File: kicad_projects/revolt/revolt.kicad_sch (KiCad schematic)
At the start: 0 parts

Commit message: add matrix to the schematic, minus the net names
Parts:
- added D1, D10, D11, D12, D13, D14, D15, D16, D17, D18, D19, D2, D20, D21, D22, D23, D24, D25, D26, D27, D28, D29, D3, D30, D31, D32, D33, D34, D4, D5, D6, D7, D8, D9: D, symbol Device:D
- added S1, S10, S11, S12, S13, S14, S15, S16, S17, S18, S19, S2, S20, S21, S22, S23, S24, S25, S26, S27, S28, S29, S3, S30, S31, S32, S33, S34, S4, S5, S6, S7, S8, S9: SW_Push_45deg, symbol Switch:SW_Push_45deg
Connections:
- new net: D12.1 (K), D17.1 (K), D2.1 (K), D21.1 (K), D25.1 (K), D33.1 (K), D7.1 (K)
- new net: D33.2 (A), S33.2
- new net: S25.1, S26.1, S27.1, S28.1, S32.1
- new net: D25.2 (A), S25.2
- new net: D14.1 (K), D19.1 (K), D23.1 (K), D27.1 (K), D30.1 (K), D4.1 (K), D9.1 (K)
- new net: D30.2 (A), S30.2
- new net: S10.1, S6.1, S7.1, S8.1, S9.1
- new net: D10.2 (A), S10.2
- new net: S1.1, S2.1, S3.1, S4.1, S5.1
- new net: D5.2 (A), S5.2
- new net: S11.1, S12.1, S13.1, S14.1, S15.1
- new net: D15.2 (A), S15.2
- new net: S21.1, S22.1, S23.1, S24.1, S31.1
- new net: D22.2 (A), S22.2
- new net: D4.2 (A), S4.2
- new net: D3.2 (A), S3.2
- new net: D28.2 (A), S28.2
- new net: D14.2 (A), S14.2
- new net: D13.1 (K), D18.1 (K), D22.1 (K), D26.1 (K), D29.1 (K), D3.1 (K), D8.1 (K)
- new net: D29.2 (A), S29.2
- new net: S29.1, S30.1, S33.1, S34.1
- new net: D32.2 (A), S32.2
- new net: D1.1 (K), D11.1 (K), D16.1 (K), D31.1 (K), D32.1 (K), D34.1 (K), D6.1 (K)
- new net: D11.2 (A), S11.2
- new net: S16.1, S17.1, S18.1, S19.1, S20.1
- new net: D16.2 (A), S16.2
- new net: D21.2 (A), S21.2
- new net: D17.2 (A), S17.2
- new net: D27.2 (A), S27.2
- new net: D10.1 (K), D15.1 (K), D20.1 (K), D24.1 (K), D28.1 (K), D5.1 (K)
- new net: D23.2 (A), S23.2
- new net: D20.2 (A), S20.2
- new net: D2.2 (A), S2.2
- new net: D6.2 (A), S6.2
- new net: D31.2 (A), S31.2
- new net: D12.2 (A), S12.2
- new net: D34.2 (A), S34.2
- new net: D26.2 (A), S26.2
- new net: D13.2 (A), S13.2
- new net: D9.2 (A), S9.2
- new net: D18.2 (A), S18.2
- new net: D7.2 (A), S7.2
- new net: D19.2 (A), S19.2
- new net: D24.2 (A), S24.2
- new net: D1.2 (A), S1.2
- new net: D8.2 (A), S8.2

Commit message: fixed pcb and schematic
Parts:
- D1, D10, D11, D12, D13, D14, D15, D16, D17, D18, D19, D2, D20, D21, D22, D23, D24, D25, D26, D27, D28, D29, D3, D30, D31, D32, D33, D34, D4, D5, D6, D7, D8, D9: value D -> ~; footprint (none) -> ComboDiode
- S1, S10, S11, S12, S13, S14, S15, S16, S17, S18, S19, S2, S20, S21, S22, S23, S24, S25, S26, S27, S28, S29, S3, S30, S31, S32, S33, S34, S4, S5, S6, S7, S8, S9: value SW_Push_45deg -> ~; footprint (none) -> keyswitches:SW_PG1350_reversible
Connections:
- net ROW3: now reaches D12.1 (K), D17.1 (K), D2.1 (K), D21.1 (K), D25.1 (K), D33.1 (K), D7.1 (K)
- net COL5: now reaches S25.1, S26.1, S27.1, S28.1, S32.1
- net ROW1: now reaches D14.1 (K), D19.1 (K), D23.1 (K), D27.1 (K), D30.1 (K), D4.1 (K), D9.1 (K)
- net COL1: now reaches S10.1, S6.1, S7.1, S8.1, S9.1
- net COL0: now reaches S1.1, S2.1, S3.1, S4.1, S5.1
- net COL2: now reaches S11.1, S12.1, S13.1, S14.1, S15.1
- net COL4: now reaches S21.1, S22.1, S23.1, S24.1, S31.1
- net ROW2: now reaches D13.1 (K), D18.1 (K), D22.1 (K), D26.1 (K), D29.1 (K), D3.1 (K), D8.1 (K)
- net COL6: now reaches S29.1, S30.1, S33.1, S34.1
- net ROW4: now reaches D1.1 (K), D11.1 (K), D16.1 (K), D31.1 (K), D32.1 (K), D34.1 (K), D6.1 (K)
- net COL3: now reaches S16.1, S17.1, S18.1, S19.1, S20.1
- net ROW0: now reaches D10.1 (K), D15.1 (K), D20.1 (K), D24.1 (K), D28.1 (K), D5.1 (K)
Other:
- moved on the sheet: D1, D10, D11, D12, D13, D14, D15, D16, D17, D18, D19, D2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

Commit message: todos, remove fp info cache
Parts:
- added J1: IDC-Header_2x07_P2.54mm_Vertical, Connector_IDC:IDC-Header_2x07_P2.54mm_Vertical, symbol Connector_Generic:Conn_02x07_Odd_Even
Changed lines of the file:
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@@
     (stroke (width 0) (type default))
+  )
+  (global_label "GND" (shape input) (at 217.17 31.75 0) (fields_autoplaced)
+    (effects (font (size 1.27 1.27)) (justify left))
+    (property "Intersheetrefs" "${INTERSHEET_REFS}" (at 224.0257 31.75 0)
+      (effects (font (size 1.27 1.27)) (justify left) hide)
+    )
+  )
+  (global_label "5V" (shape input) (at 196.85 31.75 180) (fields_autoplaced)
+    (effects (font (size 1.27 1.27)) (justify right))
+    (property "Intersheetrefs" "${INTERSHEET_REFS}" (at 191.5667 31.75 0)
+      (effects (font (size 1.27 1.27)) (justify right) hide)
+    )
   )
   (hierarchical_label "COL3" (shape input) (at 88.9 25.4 90) (fields_autoplaced)
@@
         )
       )
+    )
+  )
+  (symbol (lib_id "Connector_Generic:Conn_02x07_Odd_Even") (at 205.74 39.37 0) (unit 1)
+    (in_bom yes) (on_board yes) (dnp no) (fields_autoplaced)
+    (property "Reference" "J1" (at 207.01 25.4 0)
+      (effects (font (size 1.27 1.27)))
+    )
+    (property "Value" "IDC-Header_2x07_P2.54mm_Vertical" (at 207.01 27.94 0)
+      (effects (font (size 1.27 1.27)))
+    )
+    (property "Footprint" "Connector_IDC:IDC-Header_2x07_P2.54mm_Vertical" (at 205.74 39.37 0)
+      (effects (font (size 1.27 1.27)) hide)
+    )
+    (property "Datasheet" "~" (at 205.74 39.37 0)
+      (effects (font (size 1.27 1.27)) hide)
+    )
+    (pin "1")
+    (pin "11")
+    (pin "10")
+    (pin "12")
+    (pin "13")
+    (pin "14")
+    (pin "2")
+    (pin "3")
+    (pin "4")
+    (pin "5")
+    (pin "6")
+    (pin "7")
+    (pin "8")
+    (pin "9")
+    (instances
+      (project "revolt"
+        (path "/b3b33ac8-110b-40a8-aa44-efaba806d054"
+          (reference "J1") (unit 1)
+        )
+      )

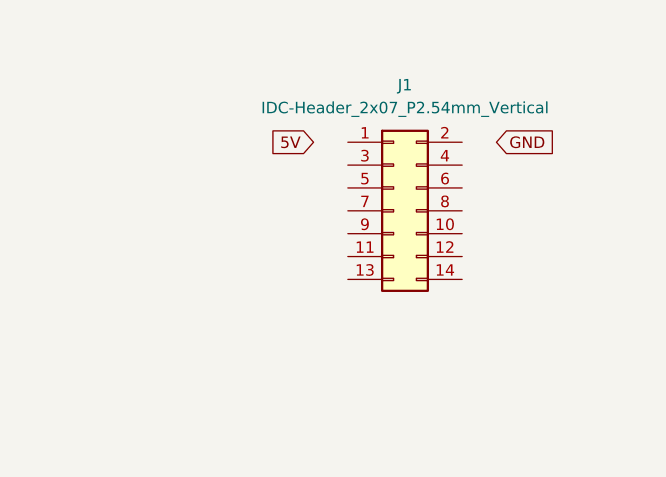
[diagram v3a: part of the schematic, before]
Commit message: Base design, need to unify and double-check DRD rules
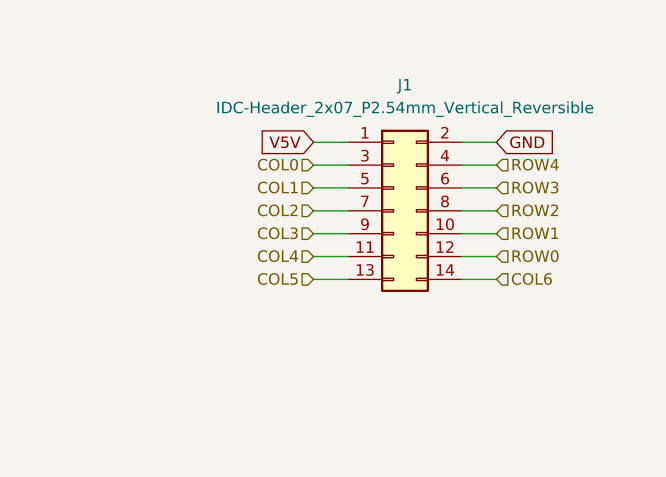
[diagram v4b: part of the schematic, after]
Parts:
- D1, D10, D11, D12, D13, D14, D15, D16, D17, D18, D19, D2, D20, D21, D22, D23, D24, D25, D26, D27, D28, D29, D3, D30, D31, D32, D33, D34, D4, D5, D6, D7, D8, D9: footprint ComboDiode -> revolt_footprints:D_SOD-123-combo-reversible
- J1: value IDC-Header_2x07_P2.54mm_Vertical -> IDC-Header_2x07_P2.54mm_Vertical_Reversible; footprint Connector_IDC:IDC-Header_2x07_P2.54mm_Vertical -> revolt_footprints:IDC-Header_2x07_P2.54mm_Vertical_Reversible
- S1, S10, S11, S12, S13, S14, S15, S16, S17, S18, S19, S2, S20, S21, S22, S23, S24, S25, S26, S27, S28, S29, S3, S30, S31, S32, S33, S34, S4, S5, S6, S7, S8, S9: footprint keyswitches:SW_PG1350_reversible -> revolt_footprints:SW_PG1350_reversible_with_keycap_outline
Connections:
- net COL0: now also J1.3 (Pin_3)
- net COL1: now also J1.5 (Pin_5)
- net COL2: now also J1.7 (Pin_7)
- net COL3: now also J1.9 (Pin_9)
- net COL4: now also J1.11 (Pin_11)
- net COL5: now also J1.13 (Pin_13)
- net COL6: now also J1.14 (Pin_14)
- net GND: now also J1.2 (Pin_2)
- net ROW0: now also J1.12 (Pin_12)
- net ROW1: now also J1.10 (Pin_10)
- net ROW2: now also J1.8 (Pin_8)
- net ROW3: now also J1.6 (Pin_6)
- net ROW4: now also J1.4 (Pin_4)
- net V5V: now reaches J1.1 (Pin_1)

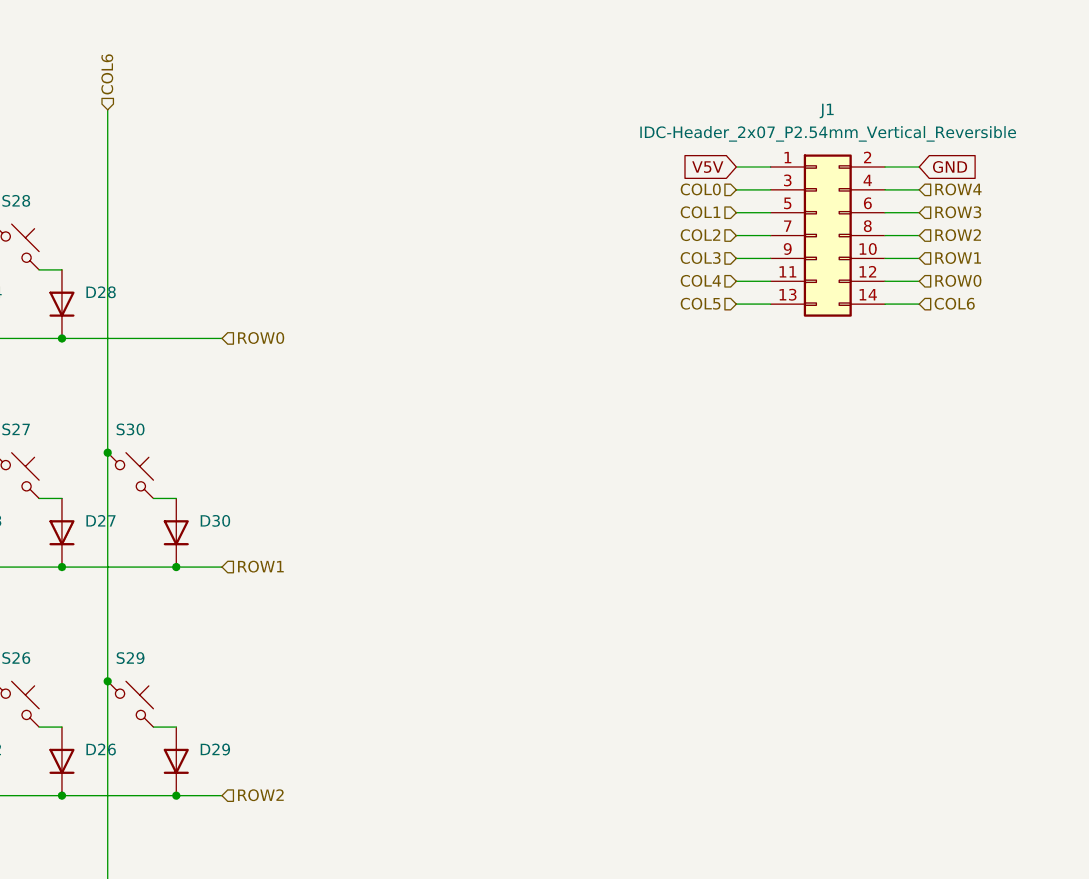
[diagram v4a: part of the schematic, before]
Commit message: Improved diodes, LED schematic
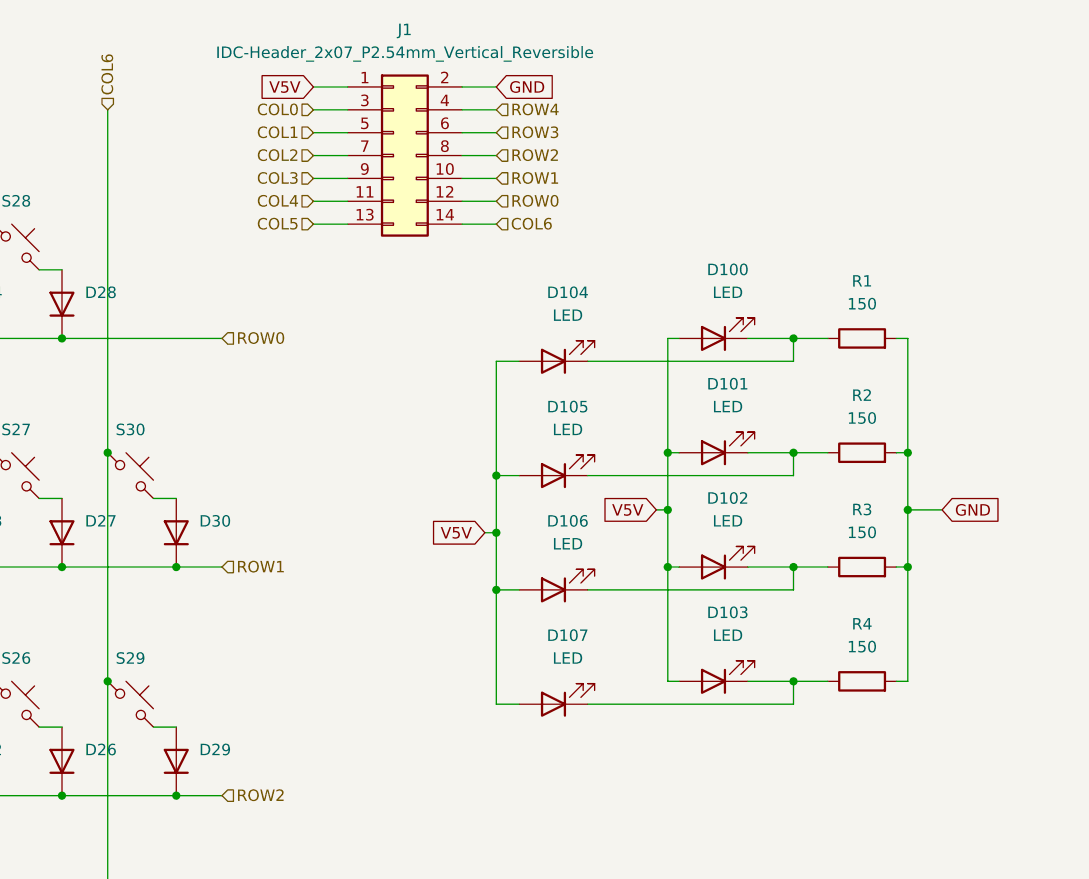
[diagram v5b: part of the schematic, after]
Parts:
- added D100, D101, D102, D103, D104, D105, D106, D107: LED, LED_SMD:LED_0805_2012Metric_Pad1.15x1.40mm_HandSolder, symbol Device:LED
- added R1, R2, R3, R4: 150, symbol Device:R
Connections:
- net GND: now also R1.2, R2.2, R3.2, R4.2
- net V5V: now also D100.2 (A), D101.2 (A), D102.2 (A), D103.2 (A), D104.2 (A), D105.2 (A), D106.2 (A), D107.2 (A)
- new net: D102.1 (K), D106.1 (K), R3.1
- new net: D103.1 (K), D107.1 (K), R4.1
- new net: D100.1 (K), D104.1 (K), R1.1
- new net: D101.1 (K), D105.1 (K), R2.1
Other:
- moved on the sheet: J1

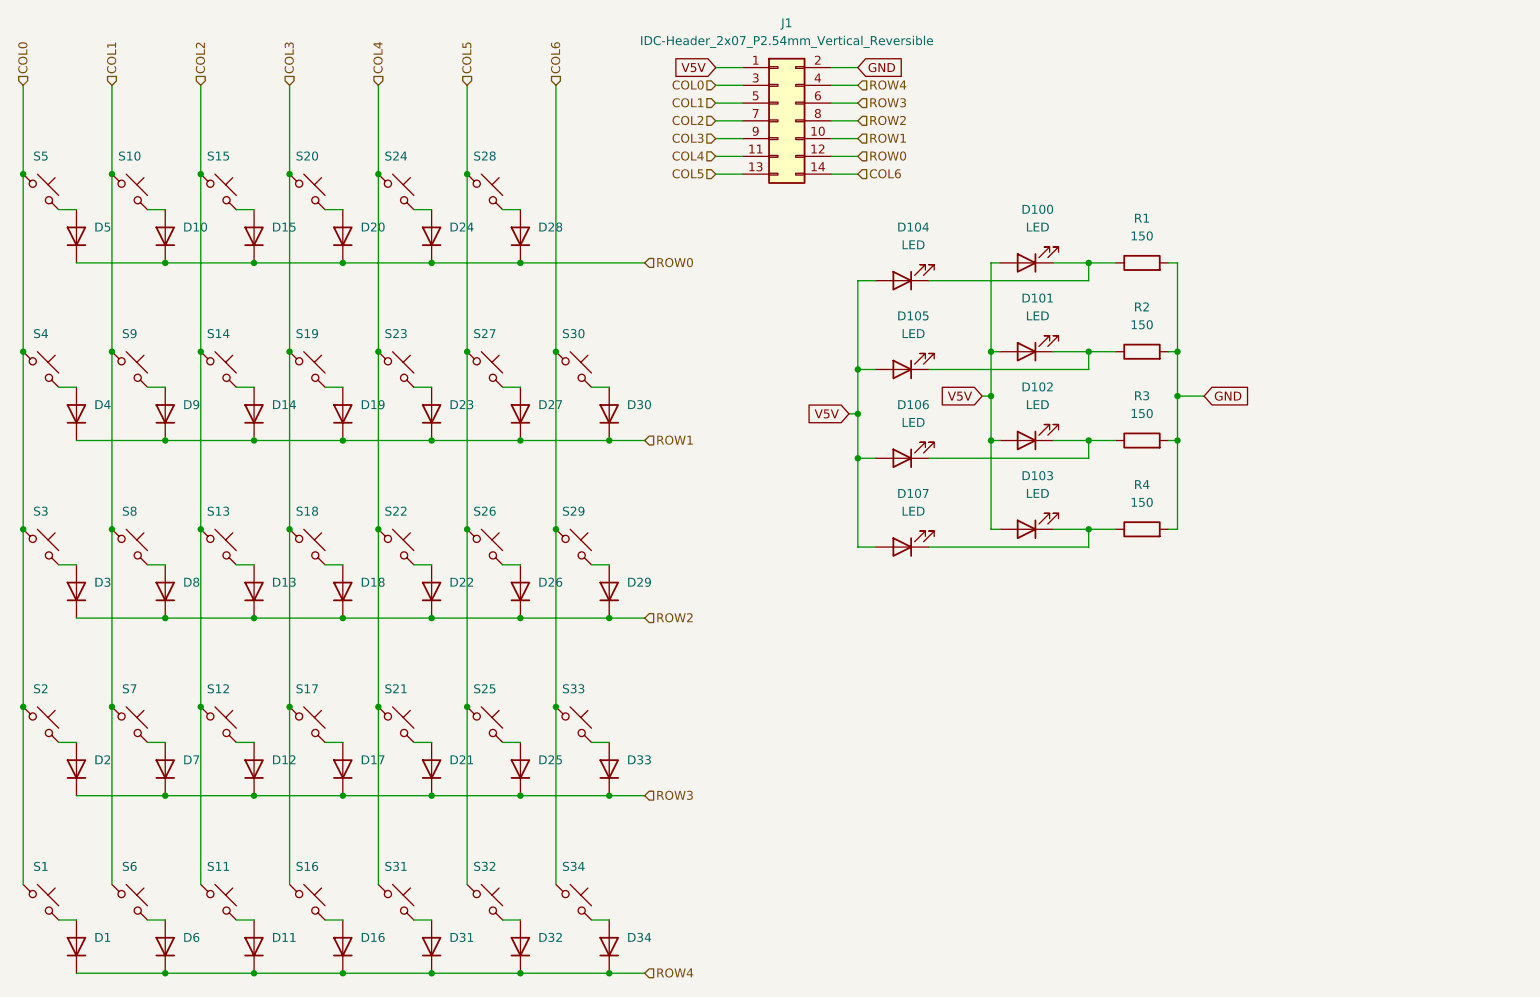
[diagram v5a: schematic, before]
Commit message: Final footprints, schematic fixes, LEDs positioned
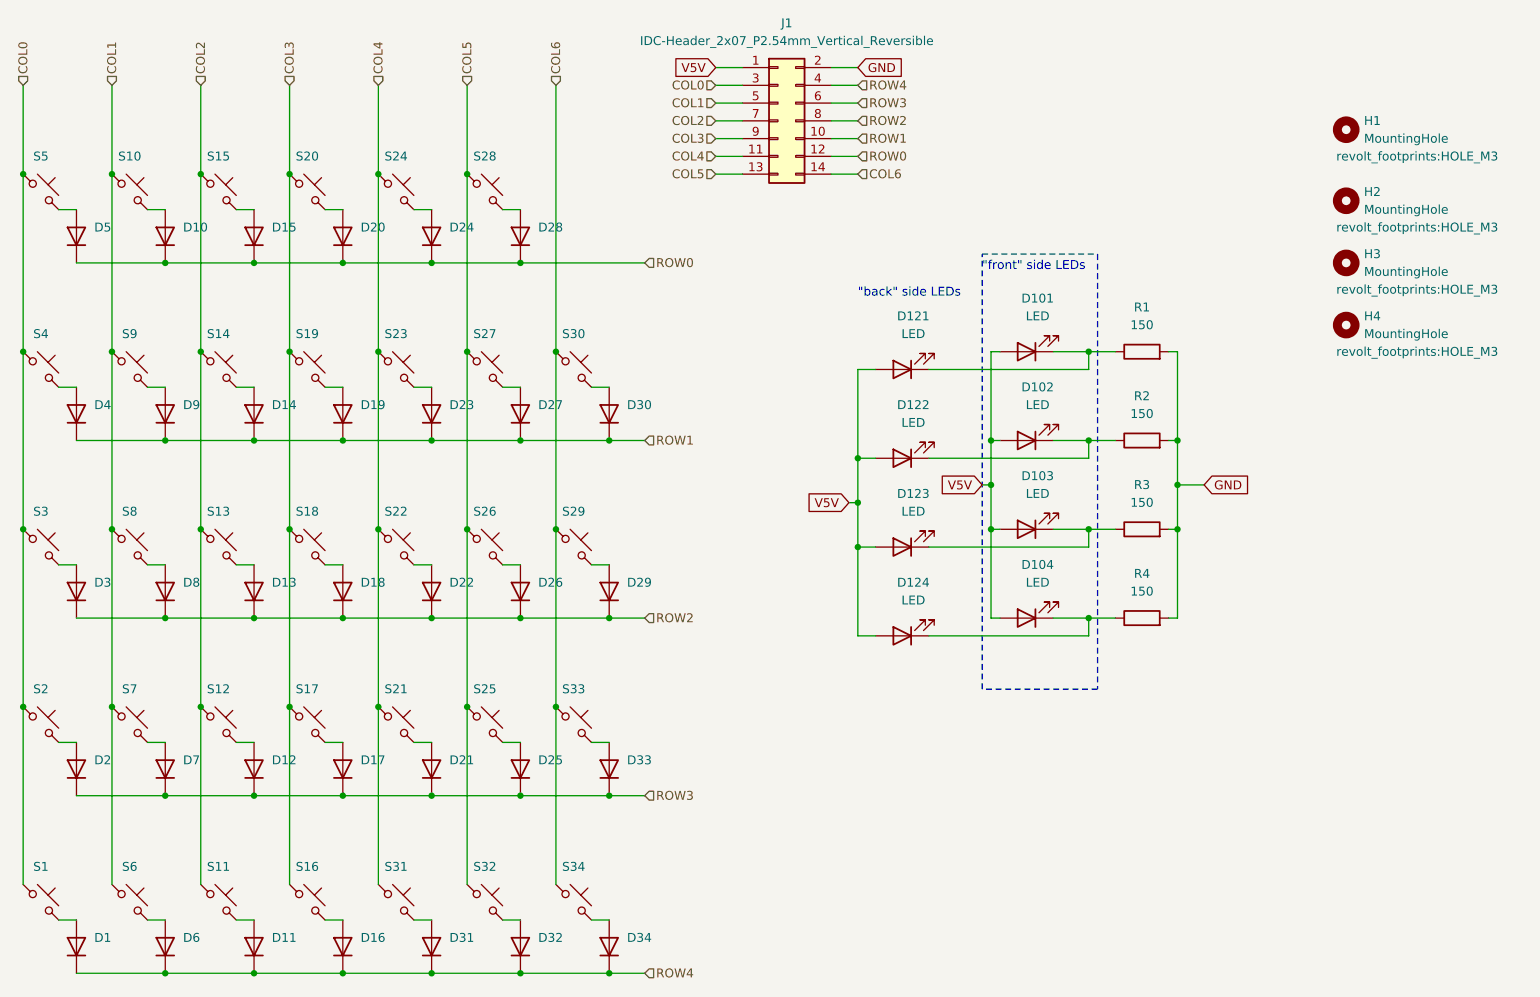
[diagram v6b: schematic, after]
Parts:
- added H1, H2, H3, H4: MountingHole, revolt_footprints:HOLE_M3, symbol Mechanical:MountingHole
- R1, R2, R3, R4: footprint (none) -> revolt_footprints:R_2512_6332Metric_Pad1.40x3.35mm_HandSolder_reversible
- renumbered D100 to D101, D101 to D102, D102 to D103, D103 to D104, D104 to D121, D105 to D122, D106 to D123, D107 to D124
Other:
- note added: ""back" side LEDs"
- note added: ""front" side LEDs"
- company: (none) -> https://github.com/nietaki/revolt-keyboard
- title: (none) -> Revolt Side PCB
- moved on the sheet: D101, D102, D103, D104, D121, D122, D123, D124, R1, R2, R3, R4

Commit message: Start routing the board
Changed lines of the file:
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@@
     )
     (property "Value" "MountingHole" (at 242.57 43.18 0)
-      (effects (font (size 1.27 1.27)) (justify left))
+      (effects (font (size 1.27 1.27)) (justify left) hide)
     )
     (property "Footprint" "revolt_footprints:HOLE_M3" (at 250.19 45.72 0)
@@
     )
     (property "Value" "MountingHole" (at 242.57 33.02 0)
-      (effects (font (size 1.27 1.27)) (justify left))
+      (effects (font (size 1.27 1.27)) (justify left) hide)
     )
     (property "Footprint" "revolt_footprints:HOLE_M3" (at 250.19 35.56 0)
@@
     )
     (property "Value" "MountingHole" (at 242.57 52.07 0)
-      (effects (font (size 1.27 1.27)) (justify left))
+      (effects (font (size 1.27 1.27)) (justify left) hide)
     )
     (property "Footprint" "revolt_footprints:HOLE_M3" (at 250.19 54.61 0)
@@
     )
     (property "Value" "MountingHole" (at 242.57 60.96 0)
-      (effects (font (size 1.27 1.27)) (justify left))
+      (effects (font (size 1.27 1.27)) (justify left) hide)
     )
     (property "Footprint" "revolt_footprints:HOLE_M3" (at 250.19 63.5 0)
